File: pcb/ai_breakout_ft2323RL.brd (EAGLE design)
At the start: 25.4 x 16.3 mm, 13 parts, among them IC1 FT2332RL, J1 1X06LONG

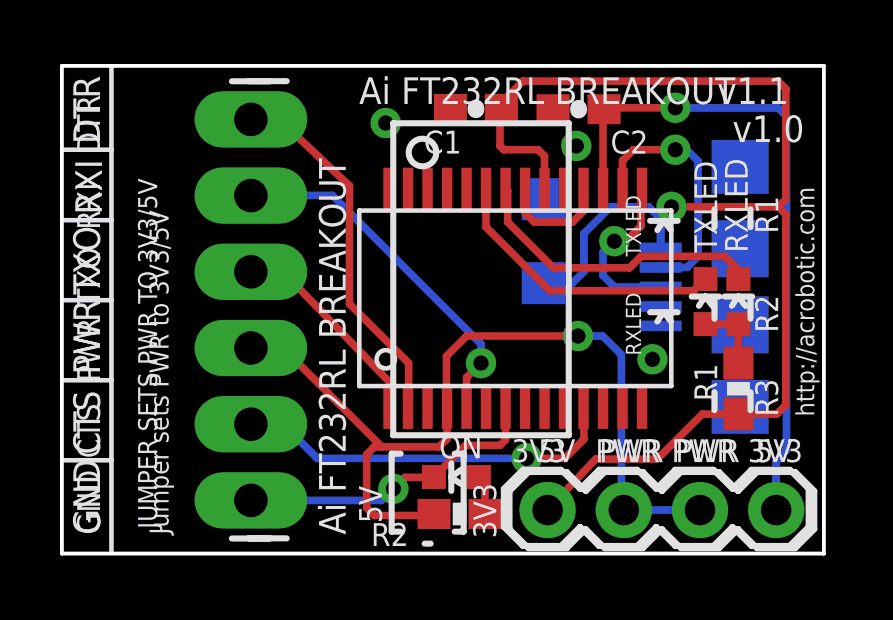
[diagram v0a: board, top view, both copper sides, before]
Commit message: Small changes in trace sizes, and silkscreen
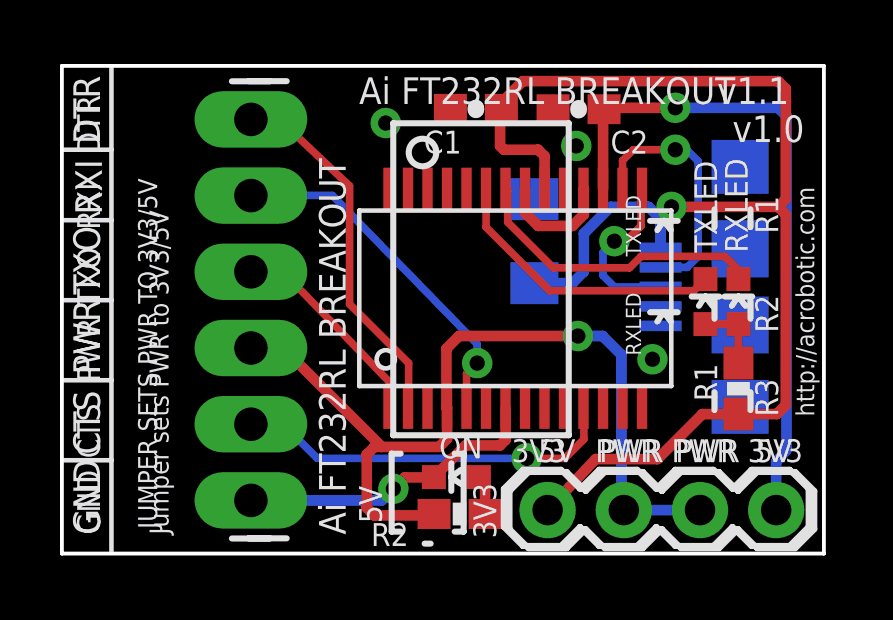
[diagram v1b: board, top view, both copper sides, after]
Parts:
- moved C3 0.38 mm to (15.7, 10.4)
